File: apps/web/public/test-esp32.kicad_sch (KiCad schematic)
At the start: 9 parts, among them J1 USB_5V, SW1 EN_BTN, U1 ESP32-WROOM-32, U2 AMS1117-3.3

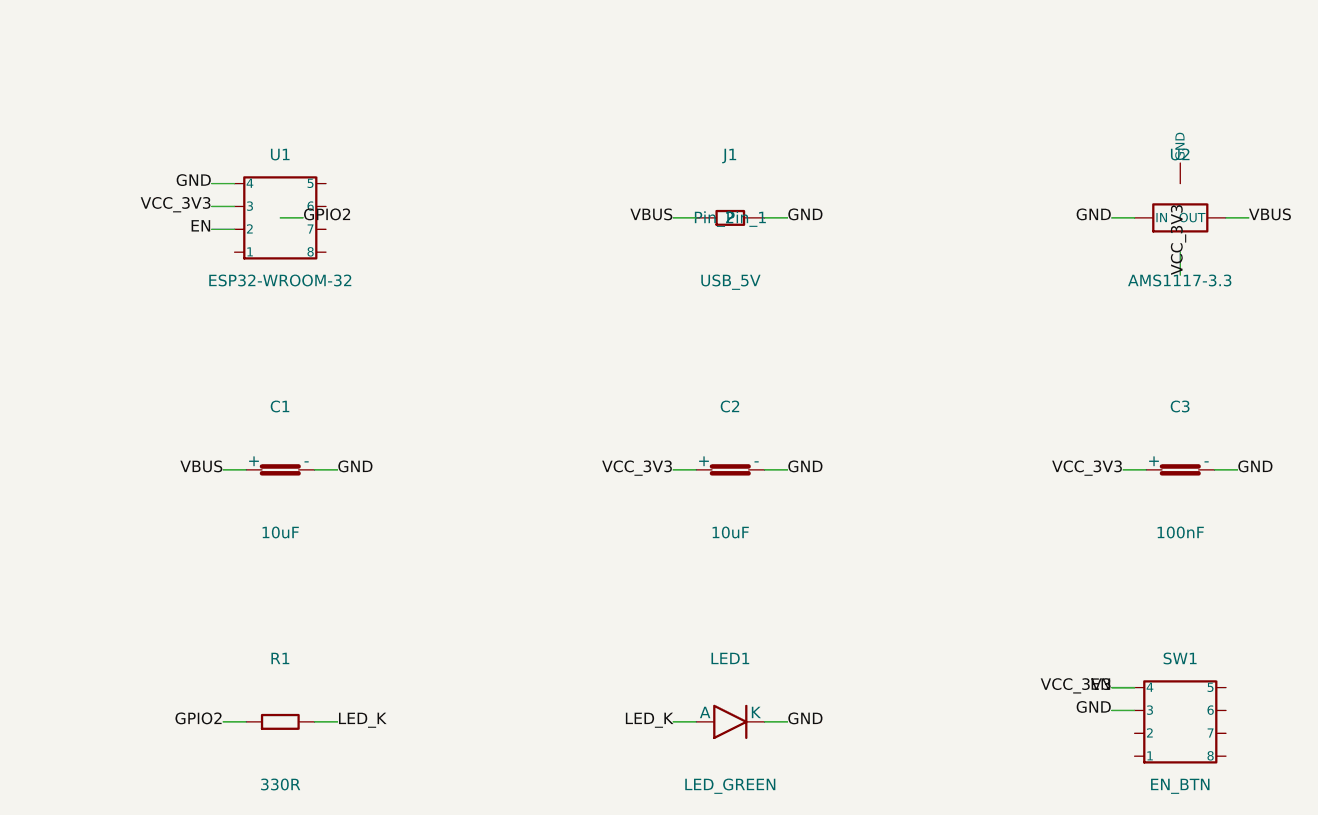
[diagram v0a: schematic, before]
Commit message: feat(kicad): Timer:NE555P named pins + compact paper for better zoom
- Add Timer:NE555P inline symbol with proper named pins:
  GND(1) TRIG(2) OUT(3) RST(4) CTRL(5) THR(6) DIS(7) VCC(8)
- _simple_lib_id: detect NE555/LM555/NA555/TLC555/ICM7555 → Timer:NE555P
- _pin_offset: Timer:NE555P reuses DIP-8 _IC_PIN_OFFSETS geometry
- Reduce paper margins 20→8mm, col_step 50→45, row_step 28→25
  LM7805 paper: 165x88 → 128x59mm (-40%) = composants 40% plus grands
  au zoom-to-fit KiCanvas
- Regenerate 3 fixtures (lm7805/ne555/esp32)
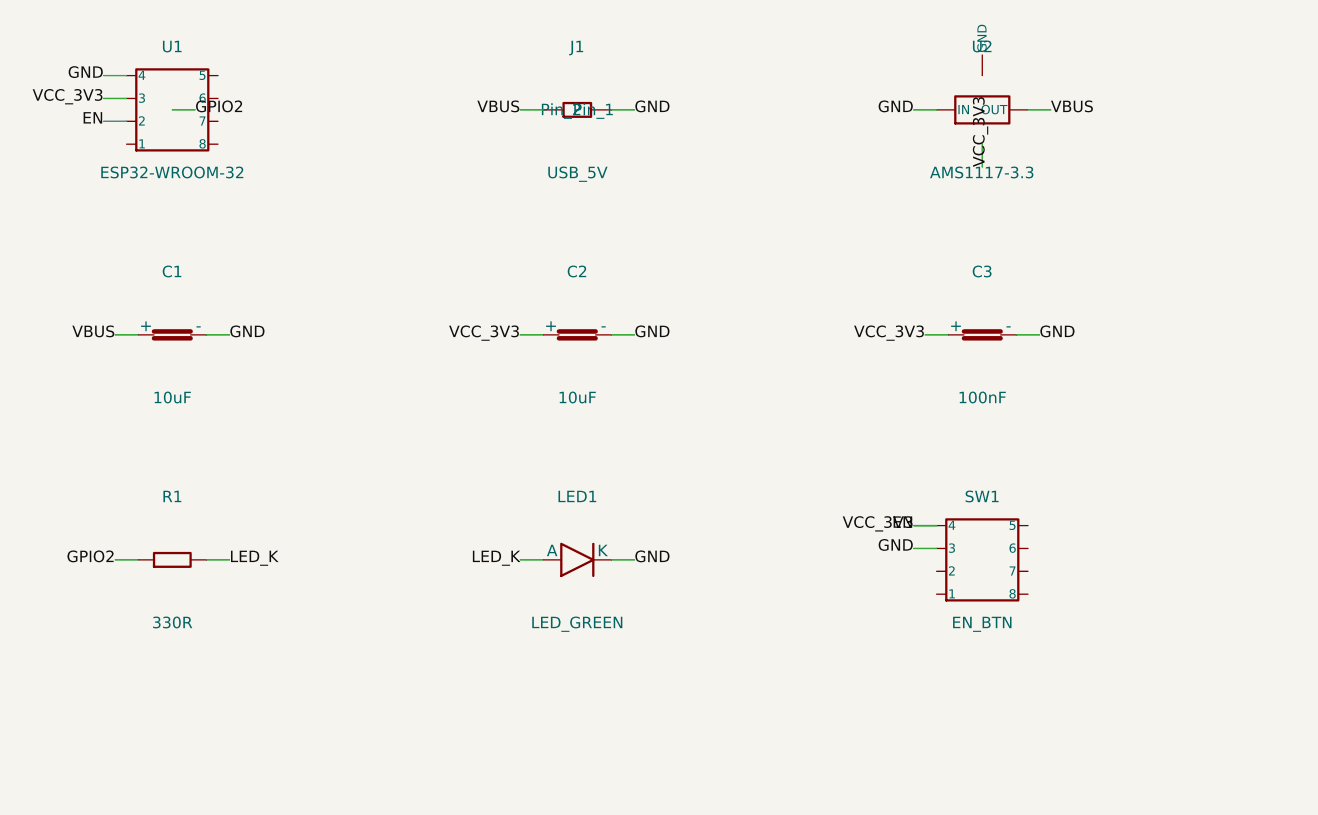
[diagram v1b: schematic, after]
